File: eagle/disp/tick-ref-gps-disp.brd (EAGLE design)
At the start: 91.4 x 106.3 mm, 53 parts, among them CN1 1PPS Out, CN2 ISP, CN3 RS232, CN4 Power In, CN5 Serial Program, U1 ATMEGA168-AU, U2 AS1115, U3 MAX232, U4 LM2931_FIXED, X1 16MHz

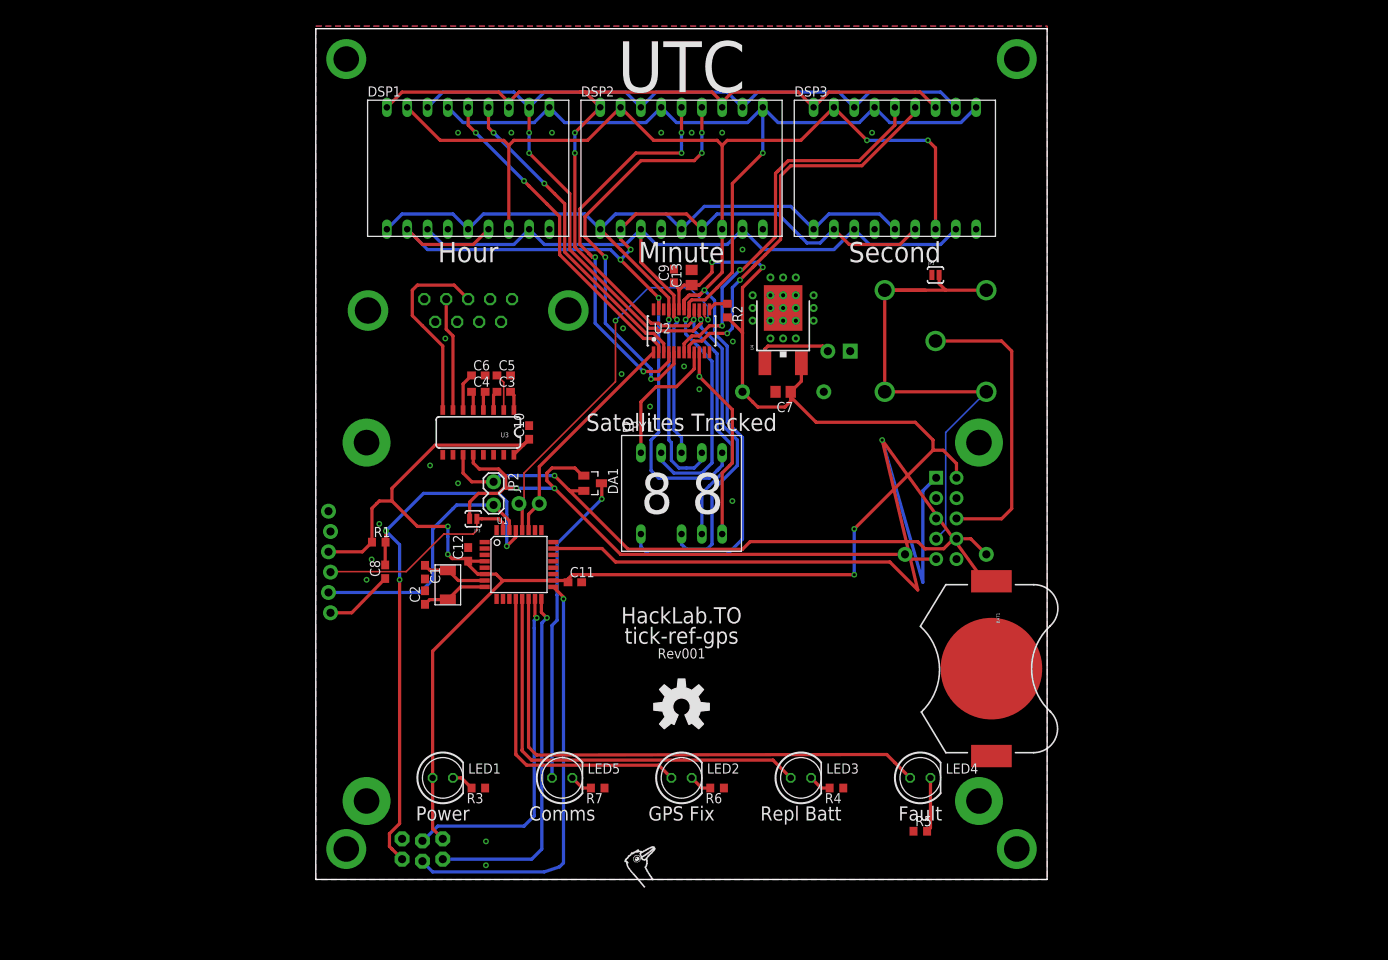
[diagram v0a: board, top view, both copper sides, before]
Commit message: Display board schematic and layout electrically done, still need to figure out mechanical design and finalize this, plus run checklists.
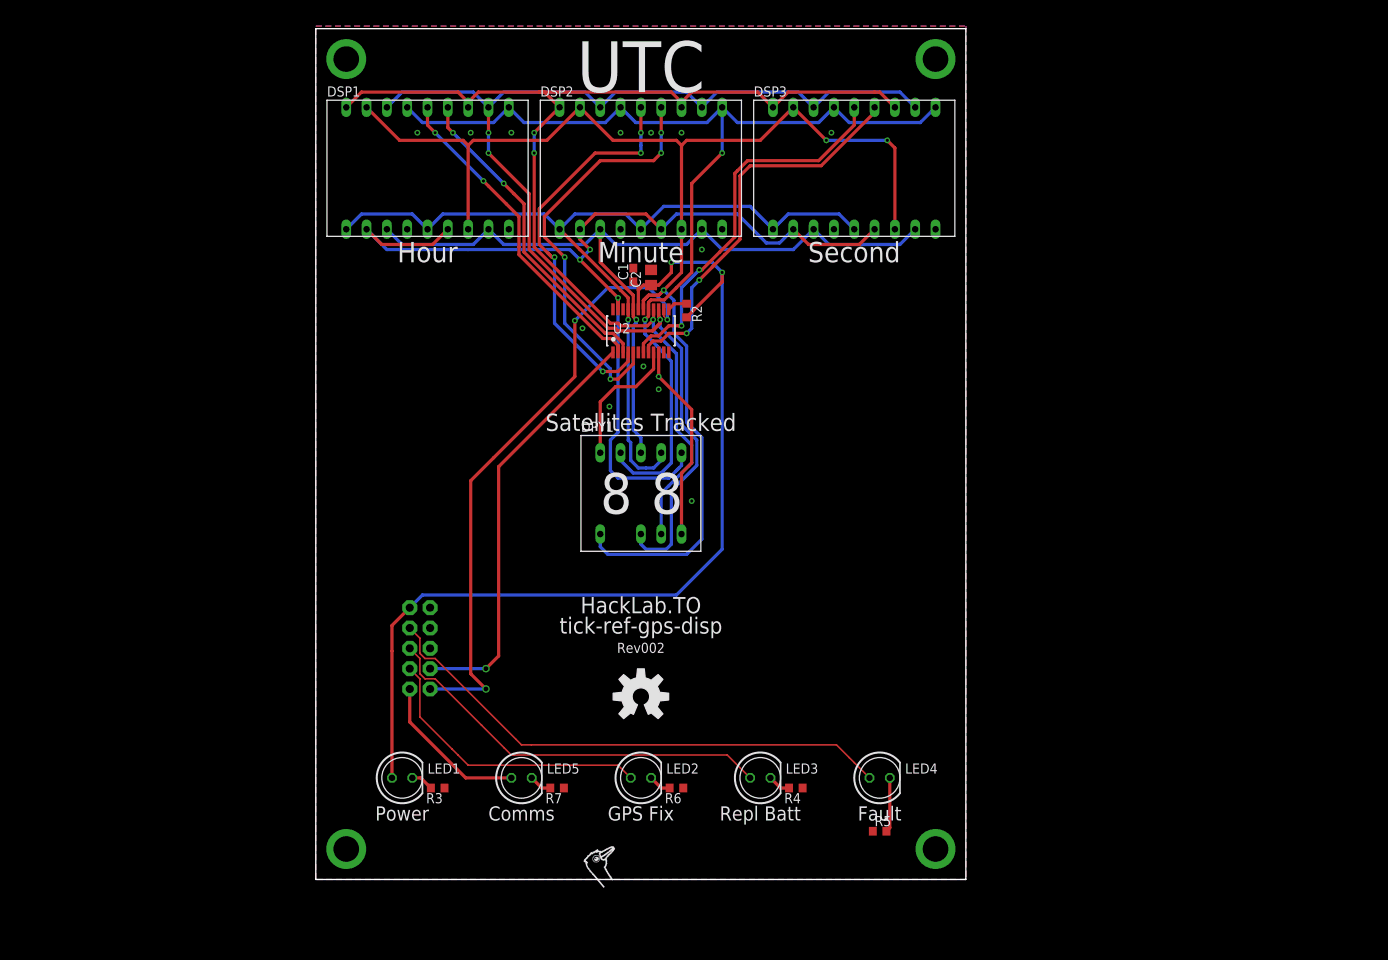
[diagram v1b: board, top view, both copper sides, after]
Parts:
- removed BAT1: CR2032, con-sen:BK-912-CR2032
- removed C10, C11, C12, C8, C9: 0.1uF, rcl:C0603
- removed C13, C7: 2.2uF, rcl:C0805
- removed C3, C4, C5, C6: 1uF, rcl:C0603
- removed CN2: ISP, SparkFun:2X3_LOCK
- removed CN3: RS232, con-subd:F09VP
- removed CN4: Power In, SparkFun:MOLEX-1X2_LOCK
- removed CN5: Serial Program, SparkFun:1X06_LOCK
- removed DA1: BAT54C, diode:SOT23
- removed GPS1: ONCORE-UT, motorola-sen:ONCORE-UT
- removed JP1: PPS RTN Link, SparkFun:SJ_2S-NO
- removed JP2: PROG/RUN, SparkFun:1X02_LOCK
- removed JP3: Standalone/PC, SparkFun:SJ_2S-NO
- removed R1: 10k, rcl:R0603
- removed TP1: GND, SparkFun:1X01
- removed TP2: +5V, SparkFun:1X01
- removed TP3: GPS In, SparkFun:1X01
- removed TP4: GPS Out, SparkFun:1X01
- removed TP5: I2C SCL, SparkFun:1X01
- removed TP6: I2C SDA, SparkFun:1X01
- removed U1: ATMEGA168-AU, Arduino-AVR:TQFP32-08
- removed U3: MAX232, SparkFun-DigitalIC:SO016
- removed U4: LM2931_FIXED, SparkFun-PowerIC:DPAK
- removed X1: 16MHz, crystal-sen:NX5032GA
- C1: value 22pF -> 0.1uF
- C2: value 22pF -> 2.2uF; device rcl:C0603 -> rcl:C0805
- CN1: value 1PPS Out -> To Main Board; device con-coax:B35N57 -> SparkFun-Connectors:AVR_ICSP
- moved CN1 75.0 mm to (13.0, 28.9), turned to 180 degrees
- moved C2 49.0 mm to (41.9, 75.2)
- moved C1 45.4 mm to (39.7, 75.6), turned to 90 degrees
- moved U$1 5.24 mm to (40.6, 22.9)
- moved R2 5.08 mm to (46.4, 71.1)
- moved R4 5.08 mm to (60.0, 11.4)
- moved DSP1 5.08 mm to (14.0, 88.9)
- moved LED1 5.08 mm to (10.8, 12.7)
- moved R3 5.08 mm to (15.2, 11.4)
- moved DPY1 5.08 mm to (40.6, 48.3)
- moved DSP2 5.08 mm to (40.6, 88.9)
- moved DSP3 5.08 mm to (67.3, 88.9)
- moved LED2 5.08 mm to (40.6, 12.7)
- moved LED3 5.08 mm to (55.6, 12.7)
- moved LED4 5.08 mm to (70.5, 12.7)
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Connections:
- removed net 1PPS: CN1.1, GPS1.6
- removed net 1PPS_RTN: CN1.2, CN1.3, CN1.4, CN1.5, GPS1.7, JP1.2
- removed net AVR_RESET: C8.2, CN2.5, R1.2, U1.29
- removed net FTDI_RTS: C8.1, CN5.6
- removed net FTDI_RX-I: CN5.4, JP3.1, U1.31
- removed net FTDI_TX-O: CN5.5, JP2.2, U1.30
- removed net GPS_RX: DA1.1, GPS1.9, JP3.2, TP3.1, U3.12
- removed net GPS_RX_HV: CN3.3, U3.8
- removed net GPS_TX: DA1.2, GPS1.8, JP2.1, TP4.1, U3.11
- removed net GPS_TX_HV: CN3.2, U3.7
- removed net ISP_MISO: CN2.1, U1.16
- removed net ISP_MOSI: CN2.4, U1.15
- removed net ISP_SCK: CN2.3, U1.17
- removed net LED5_D: DA1.3, LED5.A
- removed net MAX232-C1+: C3.2, U3.1
- removed net MAX232-C1-: C3.1, U3.3
- removed net MAX232-C2+: C4.2, U3.4
- removed net MAX232-C2-: C4.1, U3.5
- removed net MAX232-V+: C5.1, U3.2
- removed net MAX232-V-: C6.1, U3.6
- removed net VBATT: BAT1.+1, GPS1.1, U1.23
- removed net VIN: CN4.2, U4.1
- removed net VPP: GPS1.4
- removed net XTAL1: C1.1, U1.7, X1.P$2
- removed net XTAL2: C2.1, U1.8, X1.P$1
- new net LED_COMM: CN1.1, LED5.A
- net +5V: now also C1.1, C2.1, CN1.9; no longer C10.1, C11.1, C12.1, C13.1, C7.1, C9.1, CN2.2, CN5.3, GPS1.2, R1.1, TP2.1, U1.18, U1.4, U1.6, U3.16, U4.3
- net GND: now also CN1.10; no longer BAT1.-, C10.2, C11.2, C12.2, C13.2, C5.2, C6.2, C7.2, C9.2, CN2.6, CN3.5, CN4.1, CN5.1, GPS1.10, GPS1.3, GPS1.MOUNT1, GPS1.MOUNT2, GPS1.MOUNT3, GPS1.MOUNT4, JP1.1, TP1.1, U1.21, U1.3, U1.5, U3.15, U4.4
- net LED_BATT: now also CN1.5; no longer U1.13
- net LED_FAULT: now also CN1.7; no longer U1.14
- net LED_GPSFIX: now also CN1.3; no longer U1.12
- net SCL: now also CN1.2; no longer TP5.1, U1.28
- net SDA: now also CN1.4; no longer TP6.1, U1.27
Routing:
- net VBATT: track 123.4 -> 0.00 mm, vias 1 -> 0
- net +5V: track 235.7 -> 123.2 mm, vias 6 -> 2
- net GPS_RX: track 80.2 -> 0.00 mm, vias 2 -> 0
- net GPS_TX: track 76.3 -> 0.00 mm, vias 1 -> 0
- net AVR_RESET: track 72.7 -> 0.00 mm, vias 3 -> 0
- net 1PPS_RTN: track 65.8 -> 0.00 mm
- net ISP_SCK: track 53.6 -> 0.00 mm, vias 1 -> 0
- net ISP_MISO: track 44.7 -> 0.00 mm, vias 1 -> 0
- net ISP_MOSI: track 42.6 -> 0.00 mm, vias 1 -> 0
- net LED5_D: track 39.4 -> 0.00 mm, vias 1 -> 0
- net 1PPS: track 37.2 -> 0.00 mm
- net FTDI_TX-O: track 32.9 -> 0.00 mm
- net SCL: track 48.7 -> 76.6 mm, vias 2 -> 3
- net FTDI_RX-I: track 26.3 -> 0.00 mm
- net GPS_RX_HV: track 24.5 -> 0.00 mm
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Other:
- board size 91.4 x 106.3 mm -> 81.3 x 106.3 mm
- board text added: "Rev002"
- board text added: "tick-ref-gps-disp"
- board text removed: "+"
- board text removed: "-"
- board text removed: "1PPS Out"
- board text removed: "6-20VDC"
- board text removed: "ISP"
- board text removed: "RS232"
- board text removed: "Rev001"
- board text removed: "Serial Program"
- board text removed: "tick-ref-gps"

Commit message: Schematic done for rev003 of the DISP board, 20 airwires left.
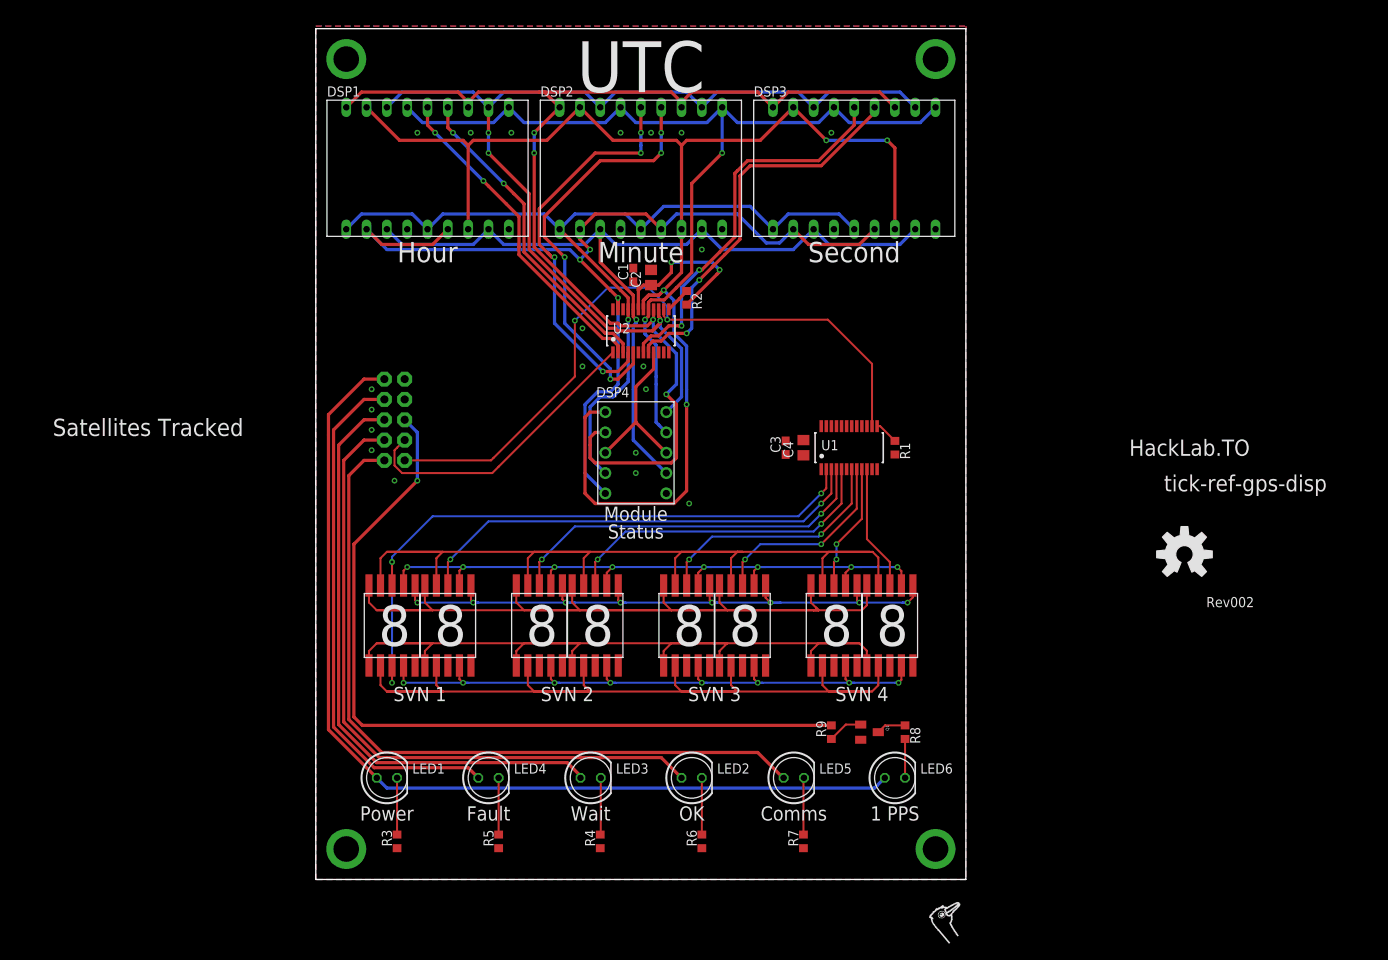
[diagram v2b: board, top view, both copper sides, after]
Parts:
- removed DPY1: Sats Tracked, led-sen:LDD-F302NI
- added C3: 0.1uF, rcl:C0603
- added C4: 2.2uF, rcl:C0805
- added DSP10: SV ID 3b, led-sen:KINGBRIGHT-ACSA02
- added DSP11: SV ID 4a, led-sen:KINGBRIGHT-ACSA02
- added DSP12: SV ID 4b, led-sen:KINGBRIGHT-ACSA02
- added DSP4: Status, led-7-segment:S4301B
- added DSP5: SV ID 1a, led-sen:KINGBRIGHT-ACSA02
- added DSP6: SV ID 1b, led-sen:KINGBRIGHT-ACSA02
- added DSP7: SV ID 2a, led-sen:KINGBRIGHT-ACSA02
- added DSP8: SV ID 2b, led-sen:KINGBRIGHT-ACSA02
- added DSP9: SV ID 3a, led-sen:KINGBRIGHT-ACSA02
- added LED6: 1PPS, led:LED5MM
- added Q1: MMBT3904, SparkFun:SOT23
- added R1: 15k, rcl:R0603
- added R8: 100, rcl:R0603
- added R9: 1.8k, rcl:R0603
- added U1: AS1115, austria-sen:QSOP24
- LED2: value GPS Fix -> OK
- LED3: value Replace Batt -> Wait
- moved U$1 70.2 mm to (108.6, 40.6)
- moved LED4 48.9 mm to (21.6, 12.7)
- moved R5 47.6 mm to (22.9, 4.76), turned to 90 degrees
- moved U$2 43.7 mm to (78.4, -5.97)
- moved LED5 34.0 mm to (59.8, 12.7)
- moved R7 31.5 mm to (61.0, 4.76), turned to 90 degrees
- moved CN1 28.8 mm to (9.84, 57.5)
- moved R4 25.3 mm to (35.6, 4.76), turned to 90 degrees
- moved LED3 21.2 mm to (34.4, 12.7)
- moved R3 8.38 mm to (10.2, 4.76), turned to 90 degrees
- moved R6 7.38 mm to (48.3, 4.76), turned to 90 degrees
- moved LED2 6.35 mm to (47.0, 12.7)
- moved LED1 1.90 mm to (8.89, 12.7)
- moved R2 1.59 mm to (46.4, 72.7)
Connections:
- net LED_BATT renamed LED_WAIT
- net LED_GPSFIX renamed LED_OK
- removed net CATH_SATS_LS: DPY1.5, U2.10
- removed net LED_SEG_A: DPY1.3, DSP1.11, DSP1.16, DSP2.11, DSP2.16, DSP3.11, DSP3.16, U2.15
- removed net LED_SEG_B: DPY1.9, DSP1.10, DSP1.15, DSP2.10, DSP2.15, DSP3.10, DSP3.15, U2.17
- removed net LED_SEG_C: DPY1.8, DSP1.3, DSP1.8, DSP2.3, DSP2.8, DSP3.3, DSP3.8, U2.20
- removed net LED_SEG_D: DPY1.6, DSP1.2, DSP1.6, DSP2.2, DSP2.6, DSP3.2, DSP3.6, U2.23
- removed net LED_SEG_E: DPY1.7, DSP1.1, DSP1.5, DSP2.1, DSP2.5, DSP3.1, DSP3.5, U2.21
- removed net LED_SEG_F: DPY1.4, DSP1.12, DSP1.18, DSP2.12, DSP2.18, DSP3.12, DSP3.18, U2.16
- removed net LED_SEG_G: DPY1.1, DSP1.17, DSP1.7, DSP2.17, DSP2.7, DSP3.17, DSP3.7, U2.18
- new net 1PPS: CN1.6, R9.2
- new net 1PPS_Q: Q1.1, R9.1
- new net DSP10-C: DSP10.3, DSP10.8, U1.8
- new net DSP11-C: DSP11.3, DSP11.8, U1.9
- new net DSP12-C: DSP12.3, DSP12.8, U1.10
- new net DSP5-C: DSP5.3, DSP5.8, U1.2
- new net DSP6-C: DSP6.3, DSP6.8, U1.3
- new net DSP7-C: DSP7.3, DSP7.8, U1.4
- new net DSP8-C: DSP8.3, DSP8.8, U1.5
- new net DSP9-C: DSP9.3, DSP9.8, U1.7
- new net DSPA_SEG_A: DSP1.11, DSP1.16, DSP2.11, DSP2.16, DSP3.11, DSP3.16, DSP4.10, U2.15
- new net DSPA_SEG_B: DSP1.10, DSP1.15, DSP2.10, DSP2.15, DSP3.10, DSP3.15, DSP4.9, U2.17
- new net DSPA_SEG_C: DSP1.3, DSP1.8, DSP2.3, DSP2.8, DSP3.3, DSP3.8, DSP4.7, U2.20
- new net DSPA_SEG_D: DSP1.2, DSP1.6, DSP2.2, DSP2.6, DSP3.2, DSP3.6, DSP4.5, U2.23
- new net DSPA_SEG_E: DSP1.1, DSP1.5, DSP2.1, DSP2.5, DSP3.1, DSP3.5, DSP4.4, U2.21
- new net DSPA_SEG_F: DSP1.12, DSP1.18, DSP2.12, DSP2.18, DSP3.12, DSP3.18, DSP4.2, U2.16
- new net DSPA_SEG_G: DSP1.17, DSP1.7, DSP2.17, DSP2.7, DSP3.17, DSP3.7, DSP4.1, U2.18
- new net DSPB_SEG_A: DSP10.7, DSP11.7, DSP12.7, DSP5.7, DSP6.7, DSP7.7, DSP8.7, DSP9.7, U1.15
- new net DSPB_SEG_B: DSP10.6, DSP11.6, DSP12.6, DSP5.6, DSP6.6, DSP7.6, DSP8.6, DSP9.6, U1.17
- new net DSPB_SEG_C: DSP10.4, DSP11.4, DSP12.4, DSP5.4, DSP6.4, DSP7.4, DSP8.4, DSP9.4, U1.20
- new net DSPB_SEG_D: DSP10.2, DSP11.2, DSP12.2, DSP5.2, DSP6.2, DSP7.2, DSP8.2, DSP9.2, U1.23
- new net DSPB_SEG_E: DSP10.1, DSP11.1, DSP12.1, DSP5.1, DSP6.1, DSP7.1, DSP8.1, DSP9.1, U1.21
- new net DSPB_SEG_F: DSP10.9, DSP11.9, DSP12.9, DSP5.9, DSP6.9, DSP7.9, DSP8.9, DSP9.9, U1.16
- new net DSPB_SEG_G: DSP10.10, DSP11.10, DSP12.10, DSP5.10, DSP6.10, DSP7.10, DSP8.10, DSP9.10, U1.18
- new net LED6_R: LED6.K, R8.2
- new net LED_ISET1: R1.1, U1.13
- new net N$1: Q1.3, R8.1
- net +5V: now also C3.1, C4.1, LED6.A, R1.2, U1.19
- net CATH_SATS_MS: now also DSP4.3, DSP4.8; no longer DPY1.10
- net GND: now also C3.2, C4.2, Q1.2, U1.6
- net SCL: now also U1.14
- net SDA: now also U1.1
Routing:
- net DSPA_SEG_G: track 0.00 -> 176.5 mm, vias 0 -> 4
- net LED_SEG_G: track 172.6 -> 0.00 mm, vias 3 -> 0
- net LED_SEG_A: track 154.8 -> 0.00 mm, vias 3 -> 0
- net DSPA_SEG_F: track 0.00 -> 152.7 mm, vias 0 -> 4
- net LED_SEG_F: track 148.8 -> 0.00 mm, vias 3 -> 0
- net DSPB_SEG_G: track 0.00 -> 133.4 mm
- net LED_SEG_B: track 133.3 -> 0.00 mm, vias 2 -> 0
- net LED_SEG_D: track 131.4 -> 0.00 mm, vias 3 -> 0
- net DSPA_SEG_A: track 0.00 -> 131.3 mm, vias 0 -> 3
- net DSPA_SEG_D: track 0.00 -> 125.6 mm, vias 0 -> 3
- net DSPB_SEG_F: track 0.00 -> 124.3 mm
- net DSPA_SEG_B: track 0.00 -> 120.8 mm, vias 0 -> 2
- net DSPB_SEG_D: track 0.00 -> 115.4 mm
- net DSPB_SEG_E: track 0.00 -> 111.8 mm
- net LED_SEG_E: track 110.3 -> 0.00 mm, vias 1 -> 0
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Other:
- board text added: "1 PPS"
- board text added: "Module"
- board text added: "OK"
- board text added: "SVN 1"
- board text added: "SVN 2"
- board text added: "SVN 3"
- board text added: "SVN 4"
- board text added: "Status"
- board text added: "Wait"
- board text removed: "GPS Fix"
- board text removed: "Repl Batt"
